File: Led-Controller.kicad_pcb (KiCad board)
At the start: 2 copper layers, 72.1 x 47.4 mm, 107 parts, among them J1 Program, J2 Barrel_Jack, J3 Screw_Terminal, J4 Screw_Terminal, J5 Ws2812 Conn, J6 Screw_Terminal, Q1 CSD18540Q5B, Q2 CSD18540Q5B, Q3 CSD18540Q5B, Q4 CSD18540Q5B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

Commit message: Fix::Voltage Reg and LED Pin
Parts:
- R33: value 37.4k -> 90k
- R6: value 41.2k -> 90k
- moved TP6 25.0 mm to (114.8, 104.8)
- moved J1 1.59 mm to (115.6, 101.8)
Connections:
- U3 pad 37: unconnected-(U3-IO23-Pad37) -> /IN1
- U3 pad 8: /IN1 -> unconnected-(U3-IO32-Pad8)
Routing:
- net /RX0: track 4.75 -> 7.20 mm
- net /EN: track 23.4 -> 25.4 mm
- net +3.3V: track 60.9 -> 62.6 mm
- net /TX0: track 4.22 -> 5.83 mm
- net /BOOT0: track 13.4 -> 11.9 mm
- net /IN1: track 36.1 -> 34.8 mm

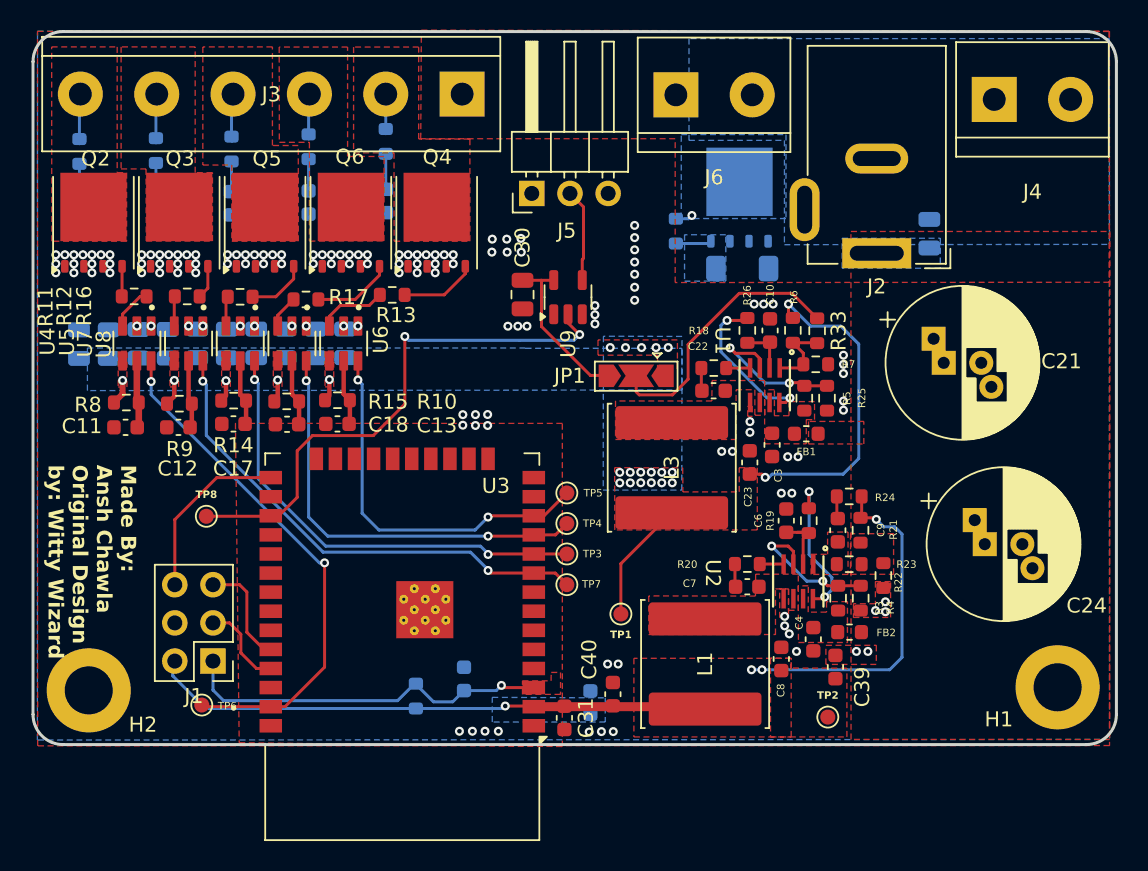
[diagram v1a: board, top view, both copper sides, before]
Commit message: Removed WS2812 Connector
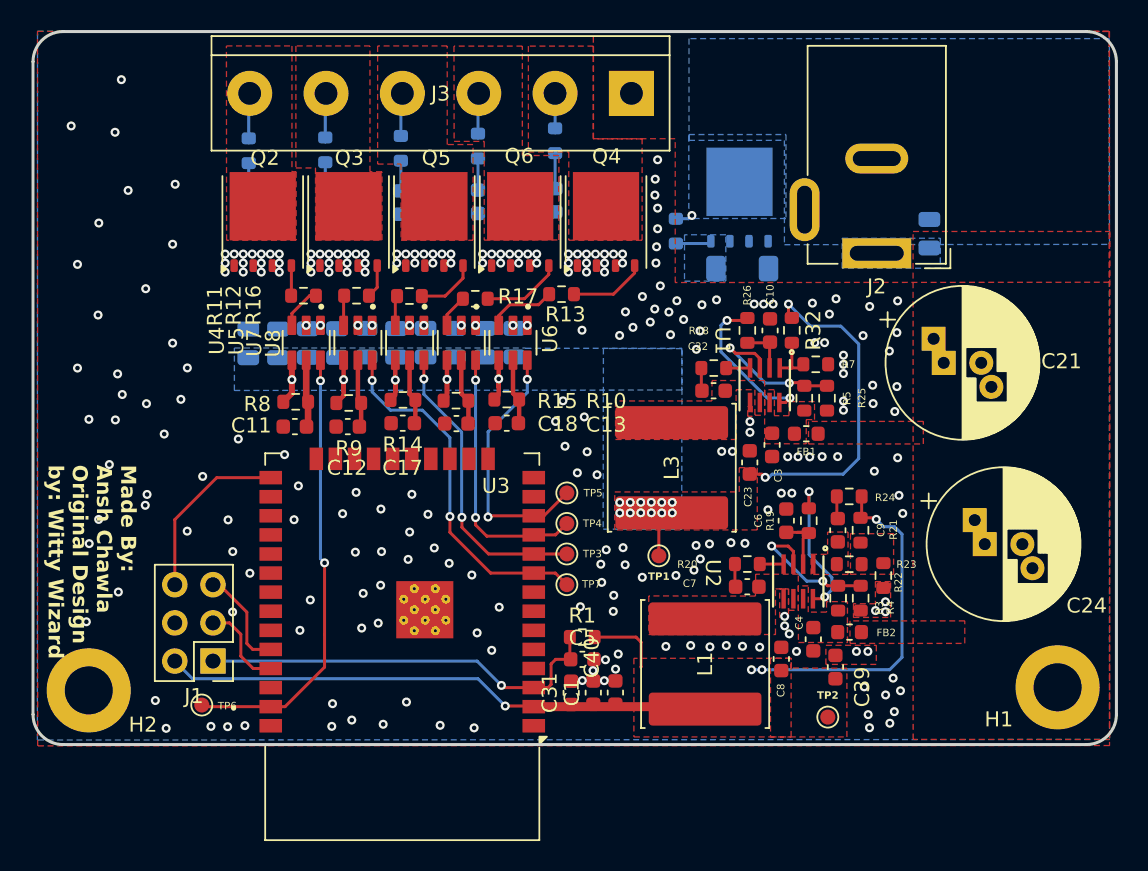
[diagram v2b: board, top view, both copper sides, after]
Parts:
- removed C30: 0.1uf, Capacitor_SMD:C_0805_2012Metric
- removed J4, J6: Screw_Terminal, TerminalBlock:TerminalBlock_bornier-2_P5.08mm
- removed J5: Ws2812 Conn, Connector_PinHeader_2.54mm:PinHeader_1x03_P2.54mm_Horizontal
- removed JP1: Jumper_3_Open, Jumper:SolderJumper-3_P2.0mm_Open_TrianglePad1.0x1.5mm
- removed R33, R6: 90k, Resistor_SMD:R_0603_1608Metric
- removed TP8: ~, TestPoint:TestPoint_Pad_D1.0mm
- removed U9: SN74LV1T34DBV, Package_TO_SOT_SMD:SOT-23-5
- added R32: 76.8k, Resistor_SMD:R_0603_1608Metric, F.Cu at (154.1, 79.8)
- C1, C5, R1: moved to F.Cu
- moved R1 11.7 mm to (140.1, 100.2), turned to 0 degrees
- moved C11 11.3 mm to (121.0, 86.2)
- moved C15 11.3 mm to (123.8, 80.7)
- moved C16 11.3 mm to (119.9, 80.7)
- moved C20 11.3 mm to (135.6, 80.6)
- moved C27 11.3 mm to (125.8, 80.6)
- moved C33 11.3 mm to (123.0, 71.3)
- moved C34 11.3 mm to (128.0, 71.3)
- moved C35 11.3 mm to (133.2, 71.3)
- moved Q5 11.3 mm to (130.3, 72.6)
- moved Q6 11.3 mm to (136.0, 72.6)
- moved R15 11.3 mm to (131.7, 84.5)
- moved R30 11.3 mm to (133.2, 67.6)
- moved R31 11.3 mm to (138.3, 67.2)
- moved R9 11.3 mm to (124.6, 84.7)
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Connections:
- U3 pad 27: /DOUT -> unconnected-(U3-IO16-Pad27)
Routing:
- net /DOUT: track 36.2 -> 0.00 mm, vias 2 -> 0
- net Net-(JP1-C): track 18.0 -> 0.00 mm
- net /IN3: track 30.7 -> 19.9 mm
- net +5V: track 10.8 -> 0.00 mm
- net /IN4: track 28.5 -> 17.9 mm
- net /IN2: track 33.3 -> 24.1 mm
- net /IN5: track 25.4 -> 17.4 mm
- net Net-(J5-Pin_2): track 6.17 -> 0.00 mm
- net /IN1: track 34.8 -> 29.9 mm
- net +9V: track 38.4 -> 42.5 mm, vias 24 -> 19
- net +3.3V: track 62.6 -> 66.6 mm
- net /EN: track 25.4 -> 27.9 mm
- net Net-(U1-FB): track 5.02 -> 3.34 mm
- net GND: vias 135 -> 259
- removed copper zone on B.Cu, net +3.3V
- removed copper zone on F.Cu, net /EN

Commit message: Did Producion changes
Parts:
- added H3: MountingHole, MountingHole:MountingHole_3.2mm_M3_DIN965_Pad, F.Cu at (107.3, 63.7)
- added H4: MountingHole, MountingHole:MountingHole_3.2mm_M3_DIN965_Pad, F.Cu at (171.8, 63.7)
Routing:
- net GND: vias 259 -> 256
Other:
- outline, holes or cut-outs redrawn
- board text added: "PROCESS NOTES: P1. SOLDERMASK BOTH SIDE: BLACK P2. SILKSCREEN BOTH SIDE PER ARTWORK. COLOUR: WHITE P3. PLATING: ENIG P4. VIA FILLING NOT REQUIRED"
- board text removed: "Made By: Ansh Chawla Original Design by: Witty Wizard"
